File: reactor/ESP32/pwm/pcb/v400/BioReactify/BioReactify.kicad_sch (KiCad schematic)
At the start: 69 parts, among them IC3 MJ5688-B111-HR1-C, IC4 MJ5688-B111-HR1-C, J10 Conn_01x06_Pin, J15 KF25C-7.62-2P, J16 KF25C-7.62-2P, J17 Conn_01x04_Pin, J18 Conn_01x02, J19 Conn_01x02, J20 Conn_01x02, J21 Conn_01x02, J22 Conn_01x02, J23 Conn_01x02, J9 Conn_01x06_Pin, Q1 IRLZ44N, Q2 IRLZ44N, Q3 IRLZ44N, Q4 IRLZ44N, Q5 IRLZ44N, Q6 IRLZ44N, SW2 SW_DIP_x01, U1 LD1117S33TR_SOT223, U10 4N25, U11 4N25, U12 4N25, U13 MAX3490xSA, U2 MCP3208, U5 ESP32-DEVKIT-V1, U6 ACS712xLCBTR-030B3, U7 4N25, U8 4N25, U9 4N25

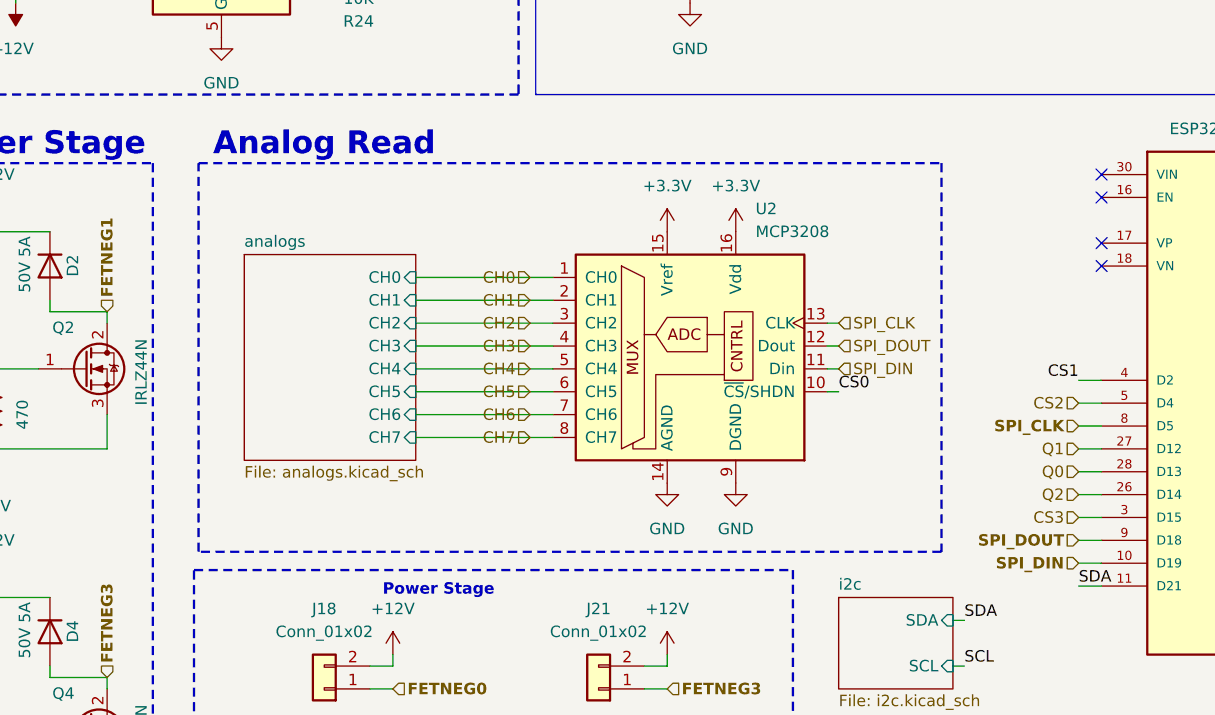
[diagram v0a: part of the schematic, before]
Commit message: Output class in cpp; Connect 2 boards to 1 experiment
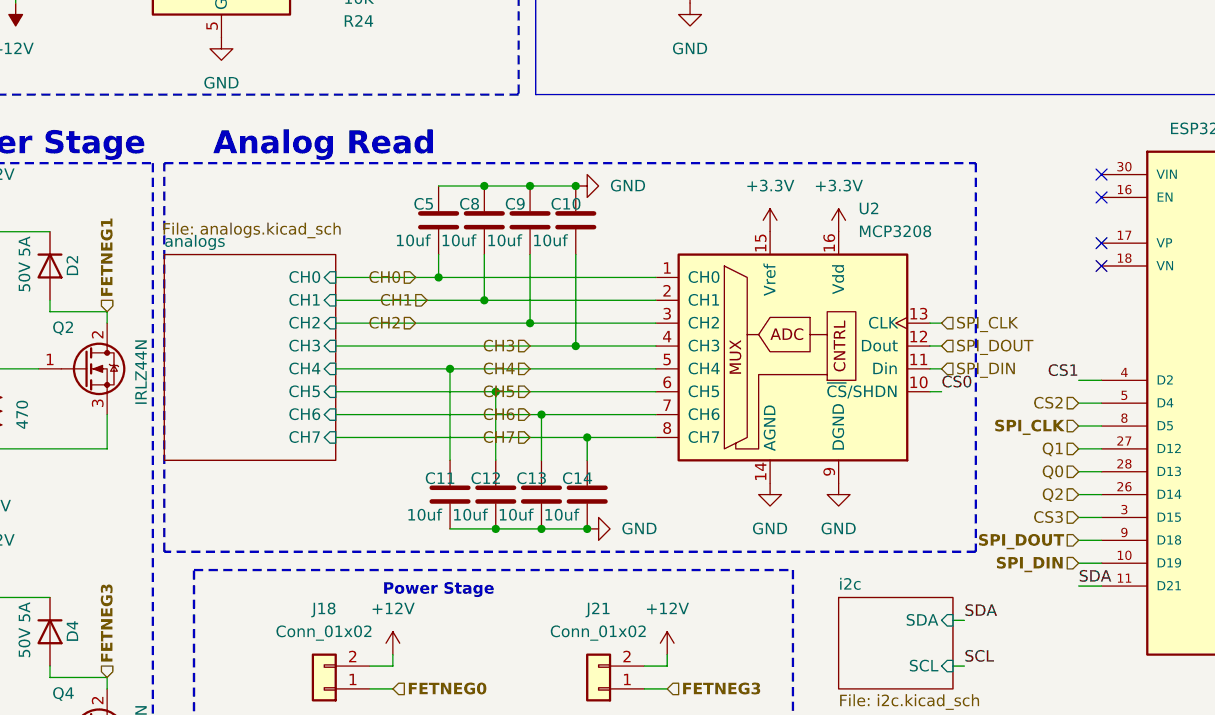
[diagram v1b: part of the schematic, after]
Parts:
- added C10, C11, C12, C13, C14, C5, C8, C9: 10uf, Capacitor_SMD:C_0603_1608Metric, symbol Device:C
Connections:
- net CH0: now also C5.2
- net CH1: now also C8.2
- net CH2: now also C9.2
- net CH3: now also C10.2
- net CH4: now also C11.1
- net CH5: now also C12.1
- net CH6: now also C13.1
- net CH7: now also C14.1
- net GND: now also C10.1, C11.2, C12.2, C13.2, C14.2, C5.1, C8.1, C9.1
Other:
- moved on the sheet: U2

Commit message: update pcb: incomplete
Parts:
- removed C10, C11, C12, C13, C14, C5, C8, C9: 10uf, Capacitor_SMD:C_0603_1608Metric, symbol Device:C
- removed C3: 10uF, Capacitor_SMD:C_0805_2012Metric, symbol Device:C_Small
- removed J15: KF25C-7.62-2P, SamacSys_Parts:KF25C7622P, symbol SamacSys_Parts:KF25C-7.62-2P
- removed SW2: SW_DIP_x01, Button_Switch_SMD:SW_DIP_SPSTx01_Slide_6.7x4.1mm_W8.61mm_P2.54mm_LowProfile, symbol Switch:SW_DIP_x01
- removed U2: MCP3208, Package_DIP:DIP-16_W7.62mm_Socket, symbol Analog_ADC:MCP3208
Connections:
- net CH0: now also U6.7 (VIOUT)
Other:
- removed sheet analogs
- added sheet adc0 (adc0.kicad_sch)
- moved on the sheet: C4, C6, C7, H3, H4, J10, J16, J18, J19, J20, J21, J22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
